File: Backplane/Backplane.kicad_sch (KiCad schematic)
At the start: 0 parts

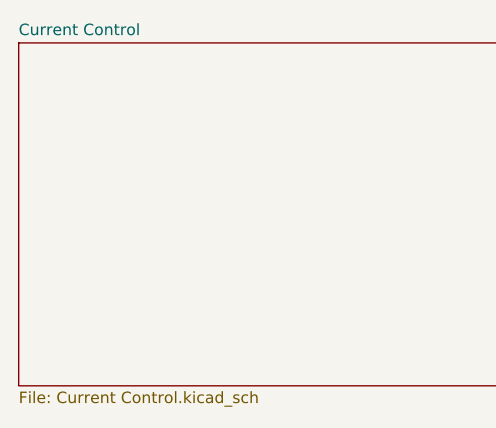
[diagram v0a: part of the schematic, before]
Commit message: Added Sheet Pins.
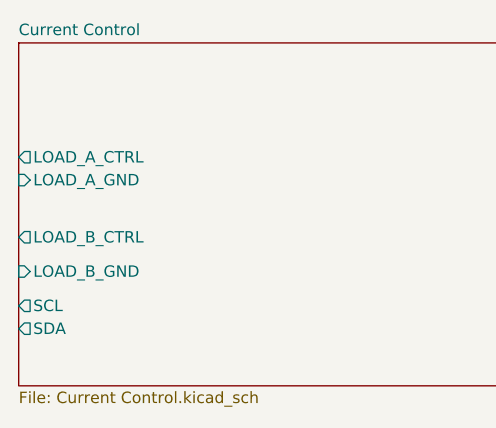
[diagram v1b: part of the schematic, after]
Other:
- sheet Current Control ports: added LOAD_A_CTRL, LOAD_A_GND, LOAD_B_CTRL, LOAD_B_GND, SCL, SDA; removed none
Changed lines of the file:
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@@
+			)
+		)
+		(pin "LOAD_A_CTRL" output
+			(at 105.41 62.23 180)
+			(effects
+				(font
+					(size 1.27 1.27)
+				)
+				(justify left)
+			)
+		)
+		(pin "LOAD_A_GND" input
+			(at 105.41 64.77 180)
+			(effects
+				(font
+					(size 1.27 1.27)
+				)
+				(justify left)
+			)
+		)
+		(pin "LOAD_B_CTRL" output
+			(at 105.41 71.12 180)
+			(effects
+				(font
+					(size 1.27 1.27)
+				)
+				(justify left)
+			)
+		)
+		(pin "LOAD_B_GND" input
+			(at 105.41 74.93 180)
+			(effects
+				(font
+					(size 1.27 1.27)
+				)
+				(justify left)
+			)
+		)
+		(pin "SCL" output
+			(at 105.41 78.74 180)
+			(effects
+				(font
+					(size 1.27 1.27)
+				)
+				(justify left)
+			)
+		)
+		(pin "SDA" output
+			(at 105.41 81.28 180)
+			(effects
+				(font
+					(size 1.27 1.27)
+				)
+				(justify left)
 			)
 		)

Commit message: Almost done with components.
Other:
- added sheet BatMax - Female (BatMax - Female.kicad_sch)
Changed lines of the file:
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@@
+		)
+	)
+	(sheet
+		(at 200.66 36.83)
+		(size 41.91 17.78)
+		(exclude_from_sim no)
+		(in_bom yes)
+		(on_board yes)
+		(dnp no)
+		(fields_autoplaced yes)
+		(stroke
+			(width 0.1524)
+			(type solid)
+		)
+		(fill
+			(color 0 0 0 0.0000)
+		)
+		(property "Sheetname" "BatMax - Female"
+			(at 200.66 36.1184 0)
+			(effects
+				(font
+					(size 1.27 1.27)
+				)
+				(justify left bottom)
+			)
+		)
+		(property "Sheetfile" "BatMax - Female.kicad_sch"
+			(at 200.66 55.1946 0)
+			(effects
+				(font
+					(size 1.27 1.27)
+				)
+				(justify left top)
+			)
+		)
+		(pin "3v3" input
+			(at 200.66 43.18 180)
+			(effects
+				(font
+					(size 1.27 1.27)
+				)
+				(justify left)
+			)
+		)
+		(pin "3V3GND" input
+			(at 200.66 44.45 180)
+			(effects
+				(font
+					(size 1.27 1.27)
+				)
+				(justify left)
+			)
+		)
+		(pin "B+" input
+			(at 200.66 48.26 180)
+			(effects
+				(font
+					(size 1.27 1.27)
+				)
+				(justify left)
+			)
+		)
+		(pin "B-" input
+			(at 200.66 52.07 180)
+			(effects
+				(font
+					(size 1.27 1.27)
+				)
+				(justify left)
+			)
+		)
+		(pin "EEPROM_WC" input
+			(at 242.57 44.45 0)
+			(effects
+				(font
+					(size 1.27 1.27)
+				)
+				(justify right)
+			)
+		)
+		(pin "SCL" input
+			(at 242.57 46.99 0)
+			(effects
+				(font
+					(size 1.27 1.27)
+				)
+				(justify right)
+			)
+		)
+		(pin "SDA" input
+			(at 242.57 49.53 0)
+			(effects
+				(font
+					(size 1.27 1.27)
+				)
+				(justify right)
+			)
+		)
+		(pin "TEMP" output
+			(at 242.57 52.07 0)
+			(effects
+				(font
+					(size 1.27 1.27)
+				)
+				(justify right)
+			)
+		)
+		(instances
+			(project "Backplane"
+				(path "/4763d09e-4fb7-455a-b785-38411d748b6f"
+					(page "3")
+				)
+			)
 		)
 	)

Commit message: Still working on blade.
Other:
- removed sheet BatMax - Female
- removed sheet Current Control
- added sheet BatPair (BatPair.kicad_sch)
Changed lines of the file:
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@@
 	(generator "eeschema")
 	(generator_version "9.0")
-	(paper "A4")
+	(paper "A")
 	(sheet
-		(at 105.41 49.53)
-		(size 73.66 38.1)
+		(at 30.48 24.13)
+		(size 67.31 26.67)
 		(exclude_from_sim no)
 		(in_bom yes)
@@
 			(color 0 0 0 0.0000)
 		)
-		(property "Sheetname" "Current Control"
-			(at 105.41 48.8184 0)
+		(property "Sheetname" "BatPair"
+			(at 30.48 23.4184 0)
 			(effects
 				(font
@@
 			)
 		)
-		(property "Sheetfile" "Current Control.kicad_sch"
-			(at 105.41 88.2146 0)
+		(property "Sheetfile" "BatPair.kicad_sch"
+			(at 30.48 51.3846 0)
 			(effects
 				(font
@@
 			)
 		)
-		(pin "LOAD_A_CTRL" output
-			(at 105.41 62.23 180)
-			(effects
-				(font
-					(size 1.27 1.27)
-				)
-				(justify left)
-			)
-		)
-		(pin "LOAD_A_GND" input
-			(at 105.41 64.77 180)
-			(effects
-				(font
-					(size 1.27 1.27)
-				)
-				(justify left)
-			)
-		)
-		(pin "LOAD_B_CTRL" output
-			(at 105.41 71.12 180)
-			(effects
-				(font
-					(size 1.27 1.27)
-				)
-				(justify left)
-			)
-		)
-		(pin "LOAD_B_GND" input
-			(at 105.41 74.93 180)
-			(effects
-				(font
-					(size 1.27 1.27)
-				)
-				(justify left)
-			)
-		)
-		(pin "SCL" output
-			(at 105.41 78.74 180)
-			(effects
-				(font
-					(size 1.27 1.27)
-				)
-				(justify left)
-			)
-		)
-		(pin "SDA" output
-			(at 105.41 81.28 180)
-			(effects
-				(font
-					(size 1.27 1.27)
-				)
-				(justify left)
-			)
-		)
 		(instances
 			(project "Backplane"
 				(path "/4763d09e-4fb7-455a-b785-38411d748b6f"
-					(page "2")
+					(page "4")
 				)
 			)
-		)
-	)
-	(sheet
-		(at 200.66 36.83)
-		(size 41.91 17.78)
-		(exclude_from_sim no)
-		(in_bom yes)
-		(on_board yes)
-		(dnp no)
-		(fields_autoplaced yes)
-		(stroke
-			(width 0.1524)
-			(type solid)
-		)
-		(fill
-			(color 0 0 0 0.0000)
-		)
-		(property "Sheetname" "BatMax - Female"
-			(at 200.66 36.1184 0)
-			(effects
-				(font
-					(size 1.27 1.27)
-				)
-				(justify left bottom)
-			)
-		)
-		(property "Sheetfile" "BatMax - Female.kicad_sch"
-			(at 200.66 55.1946 0)
-			(effects
-				(font
-					(size 1.27 1.27)
-				)
-				(justify left top)
-			)
-		)
-		(pin "3v3" input
-			(at 200.66 43.18 180)
-			(effects
-				(font
-					(size 1.27 1.27)
-				)
-				(justify left)
-			)
-		)
-		(pin "3V3GND" input
-			(at 200.66 44.45 180)
-			(effects
-				(font
-					(size 1.27 1.27)
-				)
-				(justify left)
-			)
-		)
-		(pin "B+" input
-			(at 200.66 48.26 180)
-			(effects
-				(font
-					(size 1.27 1.27)
-				)
-				(justify left)
-			)
-		)
-		(pin "B-" input
-			(at 200.66 52.07 180)
-			(effects
-				(font
-					(size 1.27 1.27)
-				)
-				(justify left)
-			)
-		)
-		(pin "EEPROM_WC" input
-			(at 242.57 44.45 0)
-			(effects
-				(font
-					(size 1.27 1.27)
-				)
-				(justify right)
-			)
-		)
-		(pin "SCL" input
-			(at 242.57 46.99 0)
-			(effects
-				(font
-					(size 1.27 1.27)
-				)
-				(justify right)
-			)
-		)
-		(pin "SDA" input
-			(at 242.57 49.53 0)
-			(effects
-				(font
-					(size 1.27 1.27)
-				)
-				(justify right)
-			)
-		)
-		(pin "TEMP" output
-			(at 242.57 52.07 0)
-			(effects
-				(font
-					(size 1.27 1.27)
-				)
-				(justify right)
-			)
-		)
-		(instances
-			(project "Backplane"
-				(path "/4763d09e-4fb7-455a-b785-38411d748b6f"
-					(page "3")
-				)
-			)

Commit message: Done with two batteries
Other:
- sheet BatPair ports: added BAT_A+, BAT_A_CHARGE, BAT_A_SCL, BAT_A_SDA, BAT_A_SNS, BAT_A_TMP, BAT_A_WC, BAT_B+, BAT_B_CHARGE, BAT_B_SCL, BAT_B_SDA, BAT_B_SNS, BAT_B_TMP, BAT_B_WC, CC_SCL, CC_SDA; removed none
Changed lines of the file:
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@@
 	(paper "A")
 	(sheet
-		(at 30.48 24.13)
-		(size 67.31 26.67)
+		(at 87.63 59.69)
+		(size 36.83 30.48)
 		(exclude_from_sim no)
 		(in_bom yes)
@@
 		)
 		(property "Sheetname" "BatPair"
-			(at 30.48 23.4184 0)
+			(at 87.63 58.9784 0)
 			(effects
 				(font
@@
 		)
 		(property "Sheetfile" "BatPair.kicad_sch"
-			(at 30.48 51.3846 0)
+			(at 87.63 90.7546 0)
 			(effects
 				(font
@@
 			)
 		)
+		(pin "BAT_A+" input
+			(at 87.63 62.23 180)
+			(effects
+				(font
+					(size 1.27 1.27)
+				)
+				(justify left)
+			)
+		)
+		(pin "BAT_A_SCL" input
+			(at 87.63 72.39 180)
+			(effects
+				(font
+					(size 1.27 1.27)
+				)
+				(justify left)
+			)
+		)
+		(pin "BAT_A_SDA" input
+			(at 87.63 69.85 180)
+			(effects
+				(font
+					(size 1.27 1.27)
+				)
+				(justify left)
+			)
+		)
+		(pin "BAT_A_SNS" input
+			(at 124.46 69.85 0)
+			(effects
+				(font
+					(size 1.27 1.27)
+				)
+				(justify right)
+			)
+		)
+		(pin "BAT_A_TMP" input
+			(at 124.46 62.23 0)
+			(effects
+				(font
+					(size 1.27 1.27)
+				)
+				(justify right)
+			)
+		)
+		(pin "BAT_A_WC" input
+			(at 124.46 77.47 0)
+			(effects
+				(font
+					(size 1.27 1.27)
+				)
+				(justify right)
+			)
+		)
+		(pin "BAT_B_CHARGE" input
+			(at 124.46 87.63 0)
+			(effects
+				(font
+					(size 1.27 1.27)
+				)
+				(justify right)
+			)
+		)
+		(pin "BAT_B_SCL" input
+			(at 87.63 80.01 180)
+			(effects
+				(font
+					(size 1.27 1.27)
+				)
+				(justify left)
+			)
+		)
+		(pin "BAT_B_SDA" input
+			(at 87.63 77.47 180)
+			(effects
+				(font
+					(size 1.27 1.27)
+				)
+				(justify left)
+			)
+		)
+		(pin "BAT_B_SNS" input
+			(at 124.46 72.39 0)
+			(effects
+				(font
+					(size 1.27 1.27)
+				)
+				(justify right)
+			)
+		)
+		(pin "BAT_B_TMP" input
+			(at 124.46 64.77 0)
+			(effects
+				(font
+					(size 1.27 1.27)
+				)
+				(justify right)
+			)
+		)
+		(pin "BAT_B_WC" input
+			(at 124.46 80.01 0)
+			(effects
+				(font
+					(size 1.27 1.27)
+				)
+				(justify right)
+			)
+		)
+		(pin "CC_SCL" input
+			(at 87.63 87.63 180)
+			(effects
+				(font
+					(size 1.27 1.27)
+				)
+				(justify left)
+			)
+		)
+		(pin "CC_SDA" input
+			(at 87.63 85.09 180)
+			(effects
+				(font
+					(size 1.27 1.27)
+				)
+				(justify left)
+			)
+		)
+		(pin "BAT_A_CHARGE" input
+			(at 124.46 85.09 0)
+			(effects
+				(font
+					(size 1.27 1.27)
+				)
+				(justify right)
+			)
+		)
+		(pin "BAT_B+" input
+			(at 87.63 64.77 180)
+			(effects
+				(font
+					(size 1.27 1.27)
+				)
+				(justify left)
+			)
+		)

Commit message: Working on Analog Section.
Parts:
- added C15, C16: 100n, Resistor_SMD:R_1206_3216Metric_Pad1.30x1.75mm_HandSolder, symbol Device:C
- added U5, U6: ADS1115IDGSR, COMPONENTS:MSOP-10_L3.0-W3.0-P0.50-LS5.0-BL, symbol COMPONENTS:ADS1115IDGSR
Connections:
- net BatPair/BAT_A_SNS: now also U6.6 (AIN2)
- net BatPair/BAT_A_TMP: now also U5.4 (AIN0)
- net BatPair/BAT_B_SNS: now also U6.7 (AIN3)
- net BatPair/BAT_B_TMP: now also U5.5 (AIN1)
- new net +5V: C15.1, C16.1, U5.8 (VDD), U6.8 (VDD)
- new net BatPair1/BAT_A_SNS: U6.4 (AIN0), U6.5 (AIN1)
- new net BatPair1/BAT_A_TMP: U5.7 (AIN3)
- new net BatPair1/BAT_B_TMP: U5.6 (AIN2)
- new net GND: C15.2, C16.2, U5.1 (ADDR), U5.3 (GND), U6.1 (ADDR), U6.3 (GND)
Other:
- added sheet BatPair1 (BatPair.kicad_sch)

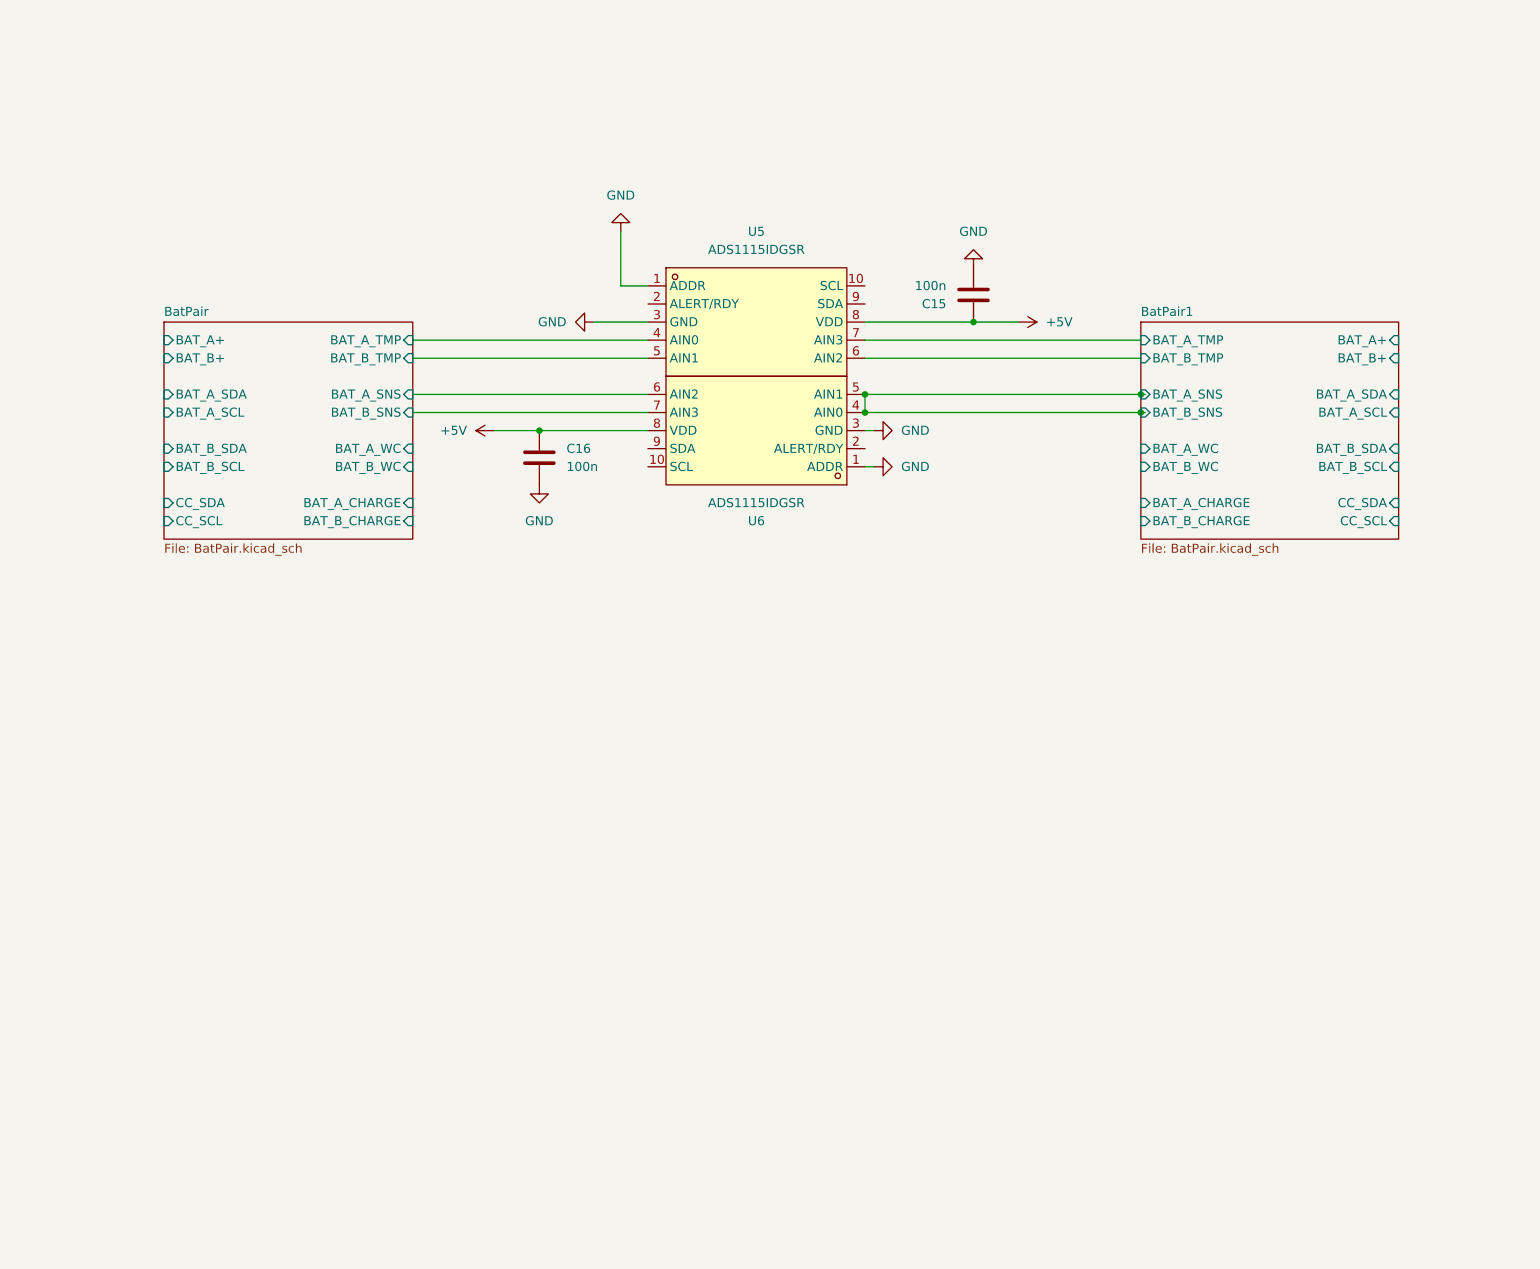
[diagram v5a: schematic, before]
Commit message: Working on splitting up I2C
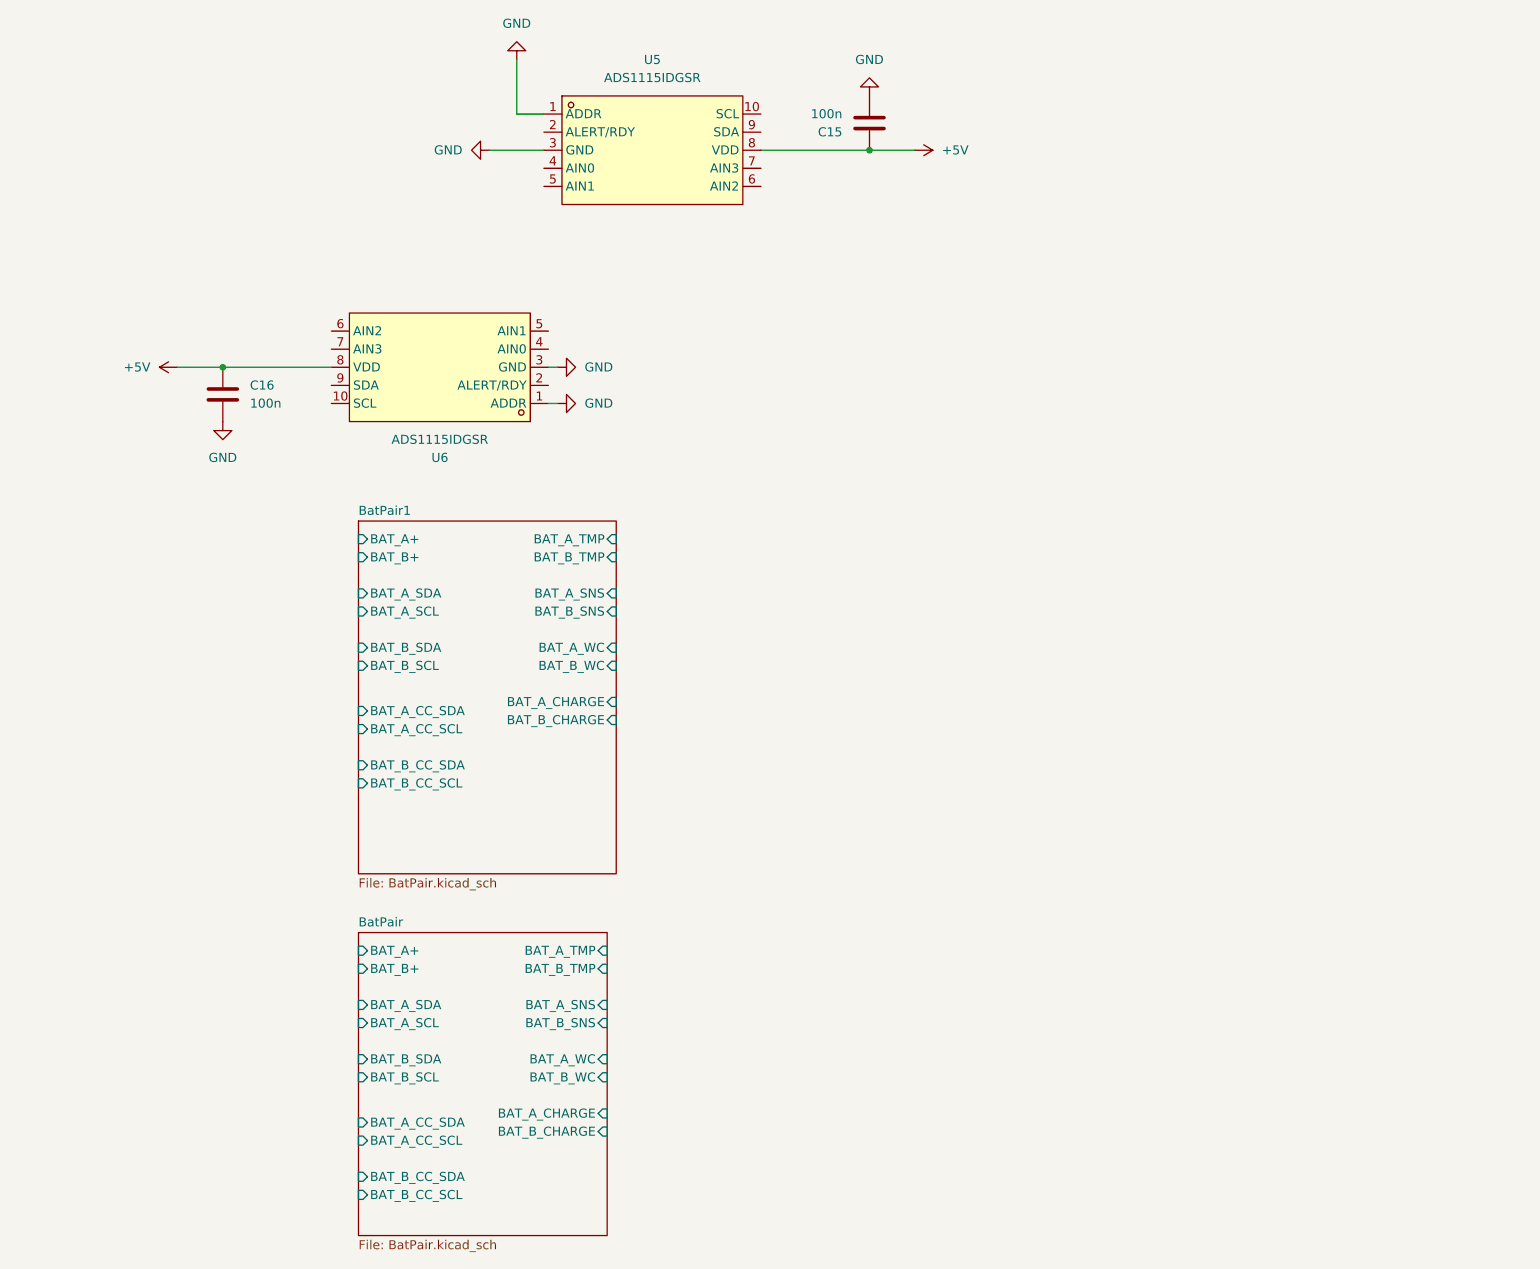
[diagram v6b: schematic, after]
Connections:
- net BatPair/BAT_A_SNS: no longer U6.6 (AIN2)
- net BatPair/BAT_A_TMP: no longer U5.4 (AIN0)
- net BatPair/BAT_B_SNS: no longer U6.7 (AIN3)
- net BatPair/BAT_B_TMP: no longer U5.5 (AIN1)
- net BatPair1/BAT_A_SNS: no longer U6.4 (AIN0), U6.5 (AIN1)
- net BatPair1/BAT_A_TMP: no longer U5.7 (AIN3)
- net BatPair1/BAT_B_TMP: no longer U5.6 (AIN2)
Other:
- sheet BatPair ports: added BAT_A_CC_SCL, BAT_A_CC_SDA, BAT_B_CC_SCL, BAT_B_CC_SDA; removed CC_SCL, CC_SDA
- sheet BatPair1 ports: added BAT_A_CC_SCL, BAT_A_CC_SDA, BAT_B_CC_SCL, BAT_B_CC_SDA; removed CC_SCL, CC_SDA
- moved on the sheet: C15, C16, U5, U6
